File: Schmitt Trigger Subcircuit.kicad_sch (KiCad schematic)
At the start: 9 parts, among them J1 Screw_Terminal_01x03, J10 Screw_Terminal_01x01, J2 Screw_Terminal_01x03, J3 Screw_Terminal_01x03, J4 Screw_Terminal_01x03, J7 Screw_Terminal_01x01, J8 Screw_Terminal_01x01, J9 Screw_Terminal_01x01, U1 74LV14

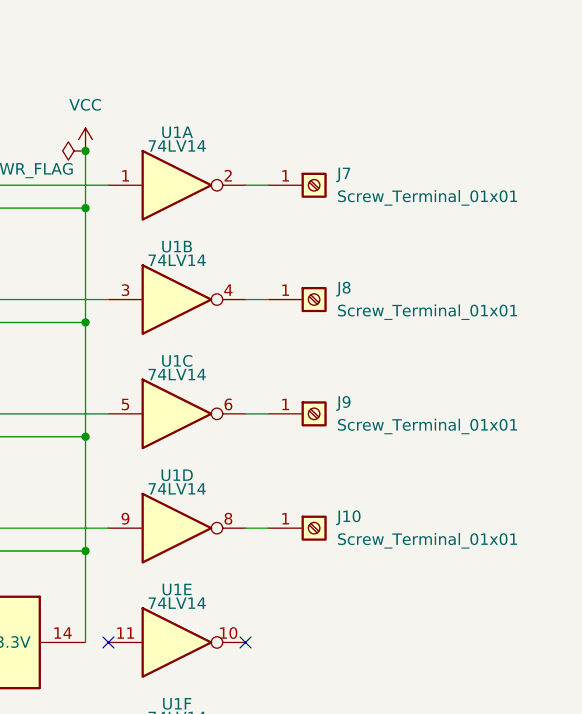
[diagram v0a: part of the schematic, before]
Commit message: Schmitt Triger Files
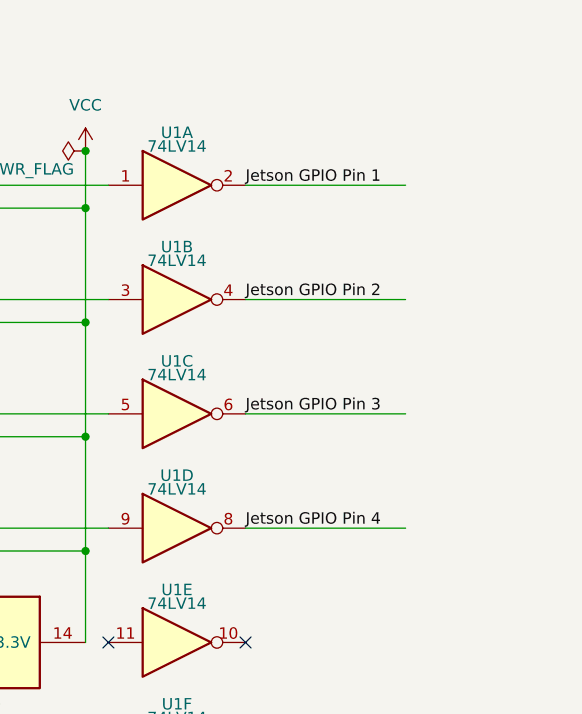
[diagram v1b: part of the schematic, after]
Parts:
- removed J10, J7, J8, J9: Screw_Terminal_01x01, TerminalBlock_MetzConnect:TerminalBlock_MetzConnect_360271_1x01_Horizontal_ScrewM3.0_Boxed, symbol Connector:Screw_Terminal_01x01
- U1: footprint Package_DIP:DIP-4_W7.62mm_Socket -> Package_DIP:DIP-12_W7.62mm
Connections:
- net Jetson GPIO Pin 1: now reaches U1.2
- net Jetson GPIO Pin 3: now reaches U1.6
- net Jetson GPIO Pin 4: now reaches U1.8
- net Jetson GPIO Pin 2: now reaches U1.4
